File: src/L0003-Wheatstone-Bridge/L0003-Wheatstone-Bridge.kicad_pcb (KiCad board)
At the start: 2 copper layers, 63.5 x 22.9 mm, 18 parts, among them P1 12V, P2 2043-1X04G00DAU, U1 MCP1703T-4002E_DB

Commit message: Finished PCB
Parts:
- moved R4 22.4 mm to (122.4, 82.0), turned to 0 degrees
- moved R5 18.3 mm to (128.0, 82.0), turned to 0 degrees
- moved R2 17.0 mm to (122.4, 89.7)
- moved TP3 15.3 mm to (125.0, 82.0)
- moved H1 14.7 mm to (133.9, 92.7)
- moved H2 14.7 mm to (133.9, 78.7)
- moved R3 12.9 mm to (128.8, 85.9), turned to 90 degrees
- moved P2 9.20 mm to (123.7, 78.0), turned to 0 degrees
- moved C2 8.95 mm to (111.8, 88.5)
- moved D1 8.67 mm to (115.8, 85.6)
- moved R1 8.64 mm to (115.8, 89.9)
- moved U1 8.64 mm to (109.5, 81.0)
- moved C1 8.50 mm to (107.2, 88.9)
- moved TP1 7.52 mm to (115.8, 79.8)
- moved P1 6.10 mm to (100.6, 81.0)
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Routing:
- net Earth: track 0.00 -> 23.4 mm, vias 0 -> 1
- net Vout-: track 31.0 -> 12.8 mm
- net +5V: track 42.2 -> 26.2 mm, vias 0 -> 1
- net Vout+: track 22.7 -> 24.0 mm, vias 0 -> 1
- net Net-(D1-Pad1): track 1.50 -> 2.00 mm
- added copper zone on B.Cu, net Earth
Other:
- board size 63.5 x 22.9 mm -> 41.4 x 19.3 mm

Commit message: Changed Wire connecting power to VRM
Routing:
- net Net-(C1-Pad2): track 9.69 -> 12.0 mm

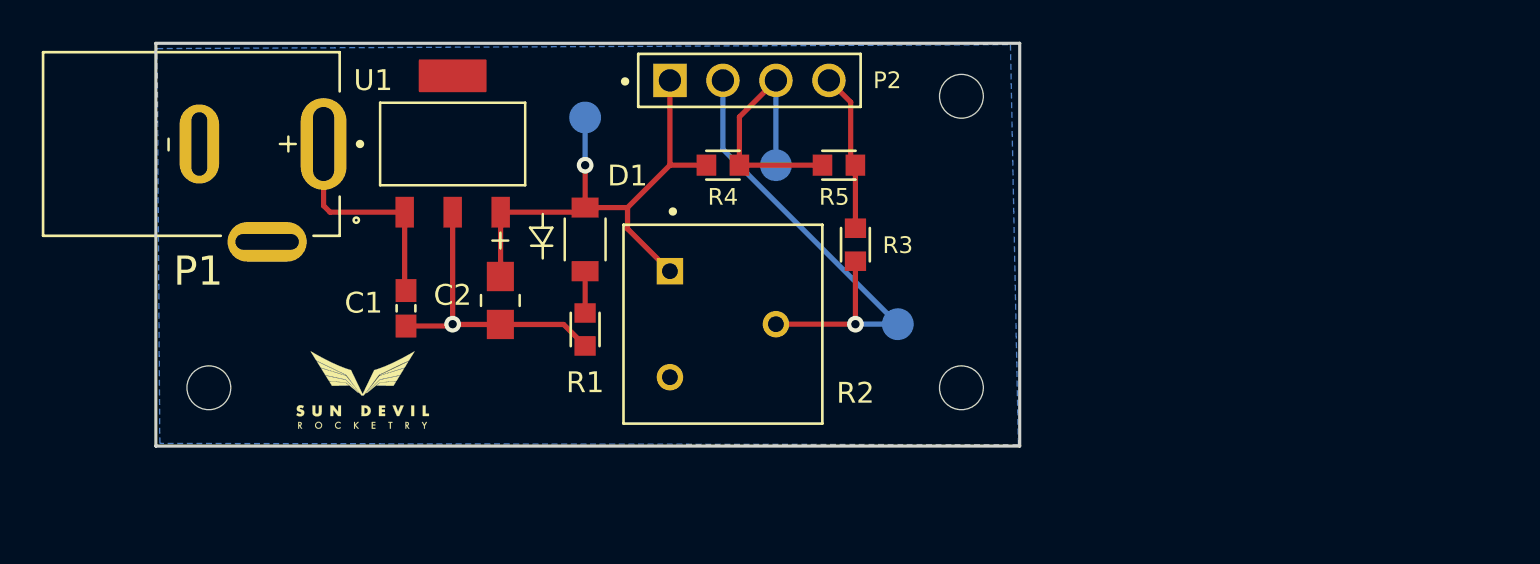
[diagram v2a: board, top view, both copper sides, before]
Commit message: added PT connectors for engine controller compatibility
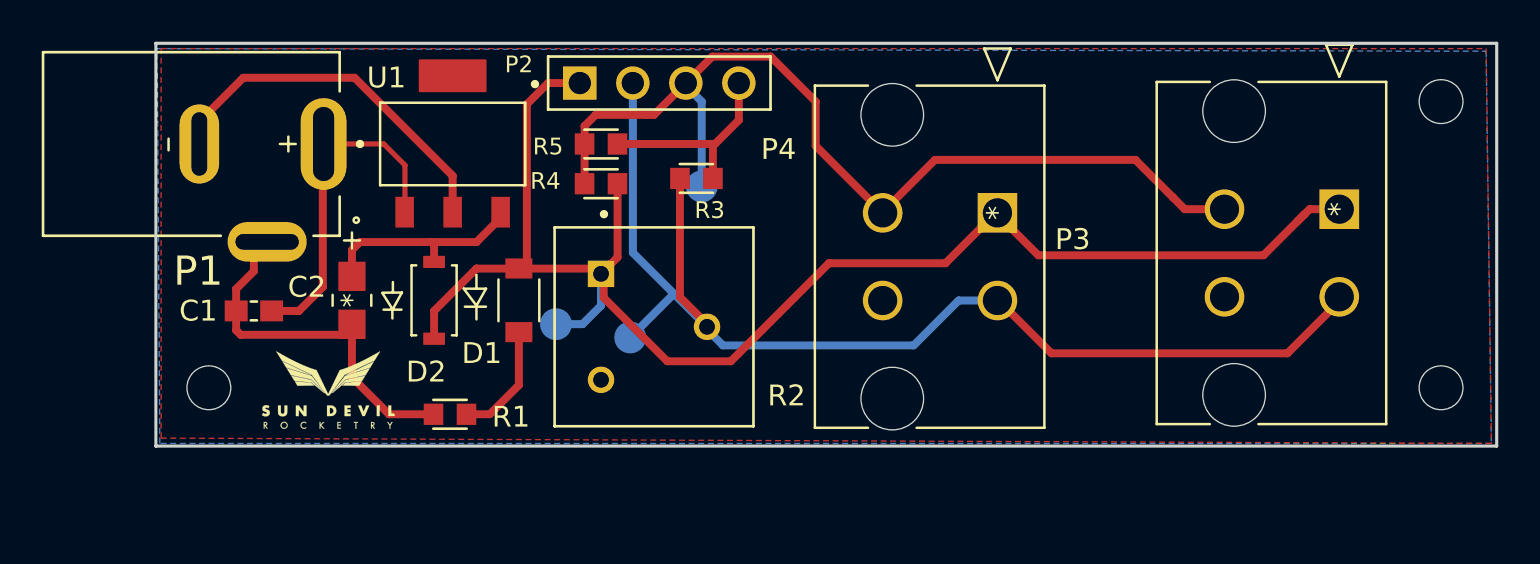
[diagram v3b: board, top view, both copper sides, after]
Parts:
- added D2: SOD-123FL_MCC, L0003-Wheatstone-Bridge:SM5819PL-TP, F.Cu at (108.6, 88.5)
- added P3: CON_39299043, L0003-Wheatstone-Bridge:39299043, F.Cu at (152.0, 84.2)
- added P4: CON_39299043, L0003-Wheatstone-Bridge:39299043, F.Cu at (135.6, 84.3)
- P2: value 2043-1X04G00DAU -> SULLINS_PPTC041LFBN-RC; footprint L0003-Wheatstone-Bridge:SULLINS_PPTC041LFBN-RC -> L0003-Wheatstone-Bridge:PPTC041LFBN-RC
- moved H2 23.0 mm to (156.8, 79.0)
- moved H1 23.0 mm to (156.8, 92.7)
- moved TP2 12.8 mm to (118.0, 90.3)
- moved R5 11.4 mm to (116.6, 81.0)
- moved TP1 10.0 mm to (114.4, 89.7)
- moved R3 8.25 mm to (121.2, 82.7), turned to 0 degrees
- moved R1 7.65 mm to (109.3, 94.0), turned to 180 degrees
- moved C1 7.29 mm to (99.9, 89.0), turned to 0 degrees
- moved C2 7.11 mm to (104.6, 88.5)
- moved R4 5.91 mm to (116.6, 82.9), turned to 180 degrees
- moved P2 4.32 mm to (119.4, 78.1)
- moved D1 4.31 mm to (112.6, 88.5)
- moved TP3 3.70 mm to (121.4, 83.1)
- moved R2 3.30 mm to (119.1, 89.8)
- moved LOGO1 1.65 mm to (103.5, 92.7)
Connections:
- C2 pad 1: +5V -> Net-(C2-Pad1)
- R2 pad 3: Net-(R2-Pad3) -> unconnected-(R2-Pad3)
- U1 pad 3: +5V -> Net-(C2-Pad1)
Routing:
- net +5V: track 26.2 -> 71.4 mm, vias 1 -> 0
- net Vout-: track 12.8 -> 45.8 mm
- net Vout+: track 24.0 -> 56.9 mm, vias 1 -> 0
- net Earth: track 23.4 -> 43.4 mm, vias 1 -> 0
- net Net-(C2-Pad1): track 0.00 -> 9.83 mm
- net Net-(C1-Pad2): track 12.0 -> 16.4 mm
- net Net-(D1-Pad1): track 2.00 -> 5.66 mm
- added copper zone on F.Cu, net Earth
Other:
- board size 41.4 x 19.3 mm -> 64.3 x 19.3 mm
- net class Default removed
- board text added: "L0003 Wheatstone Bridge Rev 2.0"
